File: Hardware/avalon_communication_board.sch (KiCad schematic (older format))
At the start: 22 parts, among them IC1 ENC28J60-I/SO, J1 RJ45_LEDS, P1 B2P-VH, Q1 FMMT597, Q2 BC817, Q3 BC817, Q4 FMMT597, Q5 BC817

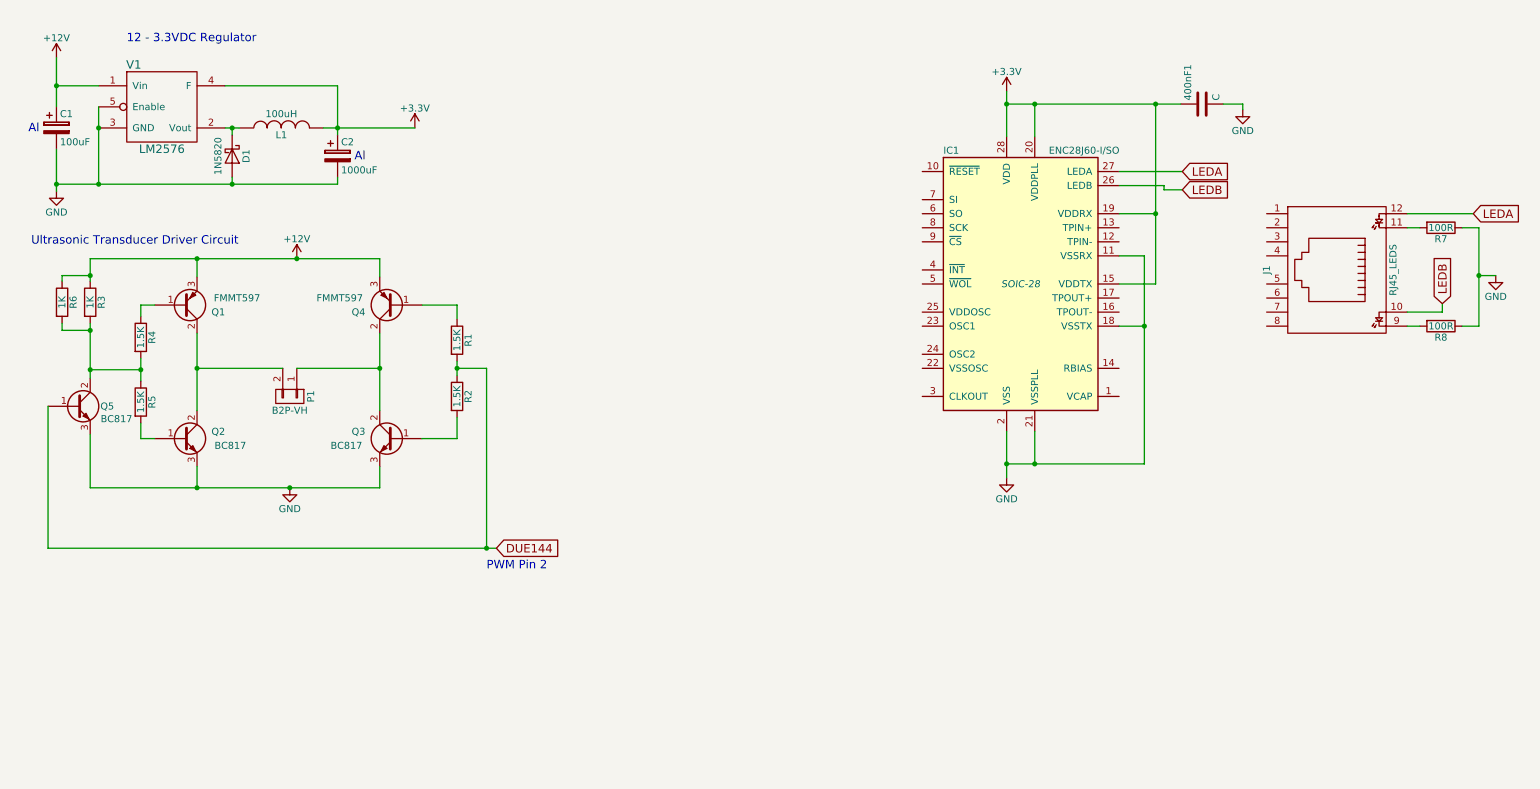
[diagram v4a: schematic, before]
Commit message: -Continued work on Ethernet Controller
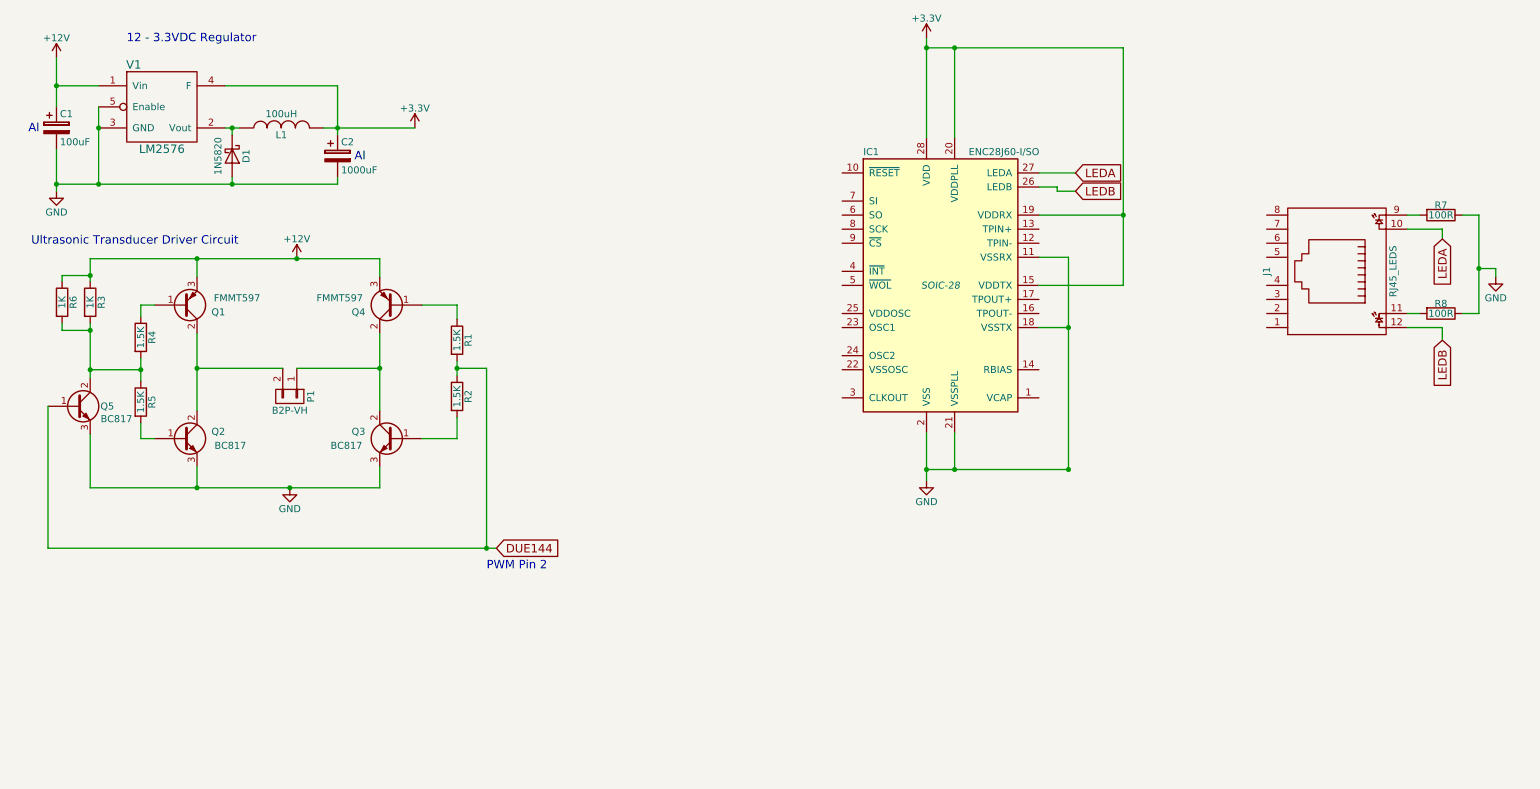
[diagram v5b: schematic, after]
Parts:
- removed 400nF1: C, symbol C
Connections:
- net LEDA: now also J1.10; no longer J1.12
- net LEDB: now also J1.12; no longer J1.10
- net at J1.11: now also R8.2; no longer R7.2
- net at J1.9: now also R7.2; no longer R8.2
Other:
- moved on the sheet: IC1, R7, R8
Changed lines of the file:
@@
 $EndComp
 Wire Wire Line
-	1040 2440 1040 2280
+	1040 2280 1040 2440
 Wire Wire Line
 	1040 2280 3100 2280
@@
 L ENC28J60-I/SO IC1
 U 1 1 5A903E11
-P 7660 2460
-F 0 "IC1" H 7110 3410 50  0000 L CNN
-F 1 "ENC28J60-I/SO" H 7860 3410 50  0000 L CNN
-F 2 "SOIC-28" H 7660 2460 50  0000 C CIN
-F 3 "" H 7660 2460 50  0000 C CNN
-	1    7660 2460
+P 7090 2470
+F 0 "IC1" H 6540 3420 50  0000 L CNN
+F 1 "ENC28J60-I/SO" H 7290 3420 50  0000 L CNN
+F 2 "SOIC-28" H 7090 2470 50  0000 C CIN
+F 3 "" H 7090 2470 50  0000 C CNN
+	1    7090 2470
 	1    0    0    -1
 $EndComp
@@
 L RJ45_LEDS J1
 U 1 1 5A9063FA
-P 9910 2360
-F 0 "J1" H 9910 1860 50  0000 C CNN
-F 1 "RJ45_LEDS" H 9910 2760 50  0000 C CNN
-F 2 "" H 9910 2310 50  0000 C CNN
-F 3 "" H 9910 2310 50  0000 C CNN
-	1    9910 2360
-	0    1    1    0
+P 9910 2370
+F 0 "J1" H 9910 1870 50  0000 C CNN
+F 1 "RJ45_LEDS" H 9910 2770 50  0000 C CNN
+F 2 "" H 9910 2320 50  0000 C CNN
+F 3 "" H 9910 2320 50  0000 C CNN
+	1    9910 2370
+	0    1    -1   0
 $EndComp
 $Comp
@@
 L +3.3V #PWR6
 U 1 1 5A908CDC
-P 7560 1090
-F 0 "#PWR6" H 7560 940 50  0001 C CNN
-F 1 "+3.3V" H 7560 1230 50  0000 C CNN
-F 2 "" H 7560 1090 50  0000 C CNN
-F 3 "" H 7560 1090 50  0000 C CNN
-	1    7560 1090
-	1    0    0    -1
-$EndComp
-Wire Wire Line
-	7560 1090 7560 1410
-Wire Wire Line
-	7760 1410 7760 1180
-Connection ~ 7560 1180
-Wire Wire Line
-	8360 1960 8620 1960
-Wire Wire Line
-	8620 1180 8620 2460
-Connection ~ 7760 1180
-Wire Wire Line
-	8620 2460 8360 2460
-Connection ~ 8620 1960
+P 6990 710
+F 0 "#PWR6" H 6990 560 50  0001 C CNN
+F 1 "+3.3V" H 6990 850 50  0000 C CNN
+F 2 "" H 6990 710 50  0000 C CNN
+F 3 "" H 6990 710 50  0000 C CNN
+	1    6990 710
+	1    0    0    -1
+$EndComp
 $Comp
 L GND #PWR7
 U 1 1 5A90B1AB
-P 7560 3840
-F 0 "#PWR7" H 7560 3590 50  0001 C CNN
-F 1 "GND" H 7560 3690 50  0000 C CNN
-F 2 "" H 7560 3840 50  0000 C CNN
-F 3 "" H 7560 3840 50  0000 C CNN
-	1    7560 3840
-	1    0    0    -1
-$EndComp
-Wire Wire Line
-	7560 3510 7560 3840
-Wire Wire Line
-	7760 3510 7760 3740
-Wire Wire Line
-	8540 3740 7560 3740
-Connection ~ 7560 3740
-Wire Wire Line
-	8540 2260 8540 3740
-Wire Wire Line
-	8540 2760 8360 2760
-Connection ~ 7760 3740
-Wire Wire Line
-	8540 2260 8360 2260
-Connection ~ 8540 2760
-Wire Wire Line
-	7560 1180 8800 1180
-$Comp
-L C 400nF1
-U 1 1 5A90F1A9
-P 8950 1180
-F 0 "400nF1" H 8975 1280 50  0000 L CNN
-F 1 "C" H 8975 1080 50  0000 L CNN
-F 2 "" H 8988 1030 50  0000 C CNN
-F 3 "" H 8950 1180 50  0000 C CNN
-	1    8950 1180
-	0    -1   -1   0
-$EndComp
-Connection ~ 8620 1180
-$Comp
-L GND #PWR8
-U 1 1 5A90F671
-P 9240 1220
-F 0 "#PWR8" H 9240 970 50  0001 C CNN
-F 1 "GND" H 9240 1070 50  0000 C CNN
-F 2 "" H 9240 1220 50  0000 C CNN
-F 3 "" H 9240 1220 50  0000 C CNN
-	1    9240 1220
-	1    0    0    -1
-$EndComp
-Wire Wire Line
-	9100 1180 9240 1180
-Wire Wire Line
-	9240 1180 9240 1220
-Text GLabel 8810 1660 2    60   Input ~ 0
+P 6990 3860
+F 0 "#PWR7" H 6990 3610 50  0001 C CNN
+F 1 "GND" H 6990 3710 50  0000 C CNN
+F 2 "" H 6990 3860 50  0000 C CNN
+F 3 "" H 6990 3860 50  0000 C CNN
+	1    6990 3860
+	1    0    0    -1
+$EndComp
+Text GLabel 8050 1670 2    60   Input ~ 0
 LEDA
-Wire Wire Line
-	8360 1660 8810 1660
-Text GLabel 8810 1790 2    60   Input ~ 0
+Text GLabel 8050 1800 2    60   Input ~ 0
 LEDB
-Wire Wire Line
-	8360 1760 8680 1760
-Wire Wire Line
-	8680 1760 8680 1790
-Wire Wire Line
-	8680 1790 8810 1790
 $Comp
 L R R7
 U 1 1 5A911D20
-P 10650 2060
-F 0 "R7" V 10730 2060 50  0000 C CNN
-F 1 "100R" V 10650 2060 50  0000 C CNN
-F 2 "" V 10580 2060 50  0000 C CNN
-F 3 "" H 10650 2060 50  0000 C CNN
-	1    10650 2060
+P 10650 1970
+F 0 "R7" V 10580 1970 50  0000 C CNN
+F 1 "100R" V 10650 1970 50  0000 C CNN
+F 2 "" V 10580 1970 50  0000 C CNN
+F 3 "" H 10650 1970 50  0000 C CNN
+	1    10650 1970
 	0    1    1    0
 $EndComp
@@
 L R R8
 U 1 1 5A91211B
-P 10650 2760
-F 0 "R8" V 10730 2760 50  0000 C CNN
-F 1 "100R" V 10650 2760 50  0000 C CNN
-F 2 "" V 10580 2760 50  0000 C CNN
-F 3 "" H 10650 2760 50  0000 C CNN
-	1    10650 2760
+P 10650 2670
+F 0 "R8" V 10580 2670 50  0000 C CNN
+F 1 "100R" V 10650 2670 50  0000 C CNN
+F 2 "" V 10580 2670 50  0000 C CNN
+F 3 "" H 10650 2670 50  0000 C CNN
+	1    10650 2670
 	0    1    1    0
 $EndComp
-Wire Wire Line
-	10410 2060 10500 2060
-Text GLabel 10880 1960 2    60   Input ~ 0
+Text GLabel 10660 2140 3    60   Input ~ 0
 LEDA
-Wire Wire Line
-	10410 1960 10880 1960
 $Comp
 L GND #PWR9
 U 1 1 5A913778
-P 11040 2400
-F 0 "#PWR9" H 11040 2150 50  0001 C CNN
-F 1 "GND" H 11040 2250 50  0000 C CNN
-F 2 "" H 11040 2400 50  0000 C CNN
-F 3 "" H 11040 2400 50  0000 C CNN
-	1    11040 2400
-	1    0    0    -1
-$EndComp
-Wire Wire Line
-	10800 2060 10920 2060
-Wire Wire Line
-	10920 2060 10920 2760
-Wire Wire Line
-	10920 2400 11040 2400
-Connection ~ 10920 2400
-Wire Wire Line
-	10920 2760 10800 2760
-Wire Wire Line
-	10500 2760 10410 2760
-Text GLabel 10660 2600 1    60   Input ~ 0
+P 11040 2410
+F 0 "#PWR9" H 11040 2160 50  0001 C CNN
+F 1 "GND" H 11040 2260 50  0000 C CNN
+F 2 "" H 11040 2410 50  0000 C CNN
+F 3 "" H 11040 2410 50  0000 C CNN
+	1    11040 2410
+	1    0    0    -1
+$EndComp
+Text GLabel 10660 2860 3    60   Input ~ 0
 LEDB
 Wire Wire Line
-	10410 2660 10660 2660
-Wire Wire Line
-	10660 2660 10660 2600
+	10410 2770 10660 2770
+Wire Wire Line
+	10660 2770 10660 2860
+Wire Wire Line
+	10920 2670 10800 2670
+Wire Wire Line
+	10800 1970 10920 1970
+Wire Wire Line
+	10920 1970 10920 2670
+Wire Wire Line
+	11040 2410 11040 2350
+Wire Wire Line
+	11040 2350 10920 2350
+Connection ~ 10920 2350
+Wire Wire Line
+	10410 2670 10500 2670
+Wire Wire Line
+	10410 1970 10500 1970
+Wire Wire Line
+	10410 2070 10660 2070
+Wire Wire Line
+	10660 2070 10660 2140
+Wire Wire Line
+	6990 780  8390 780
+Wire Wire Line
+	7790 1670 8050 1670
+Wire Wire Line
+	7790 1770 7920 1770
+Wire Wire Line
+	7920 1770 7920 1800
+Wire Wire Line
+	7920 1800 8050 1800
+Wire Wire Line
+	7790 1970 8390 1970
+Wire Wire Line
+	8390 780  8390 2470
+Wire Wire Line
+	6990 710  6990 1420
+Connection ~ 6990 780
+Wire Wire Line
+	7190 1420 7190 780
+Connection ~ 7190 780
+Wire Wire Line
+	8390 2470 7790 2470
+Connection ~ 8390 1970
+Wire Wire Line
+	6990 3520 6990 3860
+Wire Wire Line
+	7190 3520 7190 3780
+Wire Wire Line
+	8000 3780 6990 3780
+Connection ~ 6990 3780
+Wire Wire Line
+	7790 2270 8000 2270
+Wire Wire Line
+	8000 2270 8000 3780
+Wire Wire Line
+	8000 2770 7790 2770
+Connection ~ 8000 2770
+Connection ~ 7190 3780
+Connection ~ 8000 3780
 $EndSCHEMATC

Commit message: -Continued work on the ethernet controller
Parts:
- added U?: B78476A8247A003, symbol B78476A8247A003
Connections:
- net at IC1.12 (TPIN-): now also U?.3 (TD-)
- net at IC1.13 (TPIN+): now also U?.1 (TD+)
- net at IC1.16 (TPOUT-): now also U?.8 (RD-)
- net at IC1.17 (TPOUT+): now also U?.6 (RD+)
- net CAM2B: now reaches J1.4
- net at J1.5: now also U?.9 (RX-)
- net at J1.6: now also U?.11 (RX+)
- net at J1.7: now also U?.14 (TX-)
- net at J1.8: now also U?.16 (TX+)
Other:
- moved on the sheet: IC1
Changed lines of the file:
@@
 L ENC28J60-I/SO IC1
 U 1 1 5A903E11
-P 7090 2470
-F 0 "IC1" H 6540 3420 50  0000 L CNN
-F 1 "ENC28J60-I/SO" H 7290 3420 50  0000 L CNN
-F 2 "SOIC-28" H 7090 2470 50  0000 C CIN
-F 3 "" H 7090 2470 50  0000 C CNN
-	1    7090 2470
+P 6280 2470
+F 0 "IC1" H 5730 3420 50  0000 L CNN
+F 1 "ENC28J60-I/SO" H 6480 3420 50  0000 L CNN
+F 2 "SOIC-28" H 6280 2470 50  0000 C CIN
+F 3 "" H 6280 2470 50  0000 C CNN
+	1    6280 2470
 	1    0    0    -1
 $EndComp
@@
 L +3.3V #PWR6
 U 1 1 5A908CDC
-P 6990 710
-F 0 "#PWR6" H 6990 560 50  0001 C CNN
-F 1 "+3.3V" H 6990 850 50  0000 C CNN
-F 2 "" H 6990 710 50  0000 C CNN
-F 3 "" H 6990 710 50  0000 C CNN
-	1    6990 710
+P 6180 710
+F 0 "#PWR6" H 6180 560 50  0001 C CNN
+F 1 "+3.3V" H 6180 850 50  0000 C CNN
+F 2 "" H 6180 710 50  0000 C CNN
+F 3 "" H 6180 710 50  0000 C CNN
+	1    6180 710
 	1    0    0    -1
 $EndComp
@@
 L GND #PWR7
 U 1 1 5A90B1AB
-P 6990 3860
-F 0 "#PWR7" H 6990 3610 50  0001 C CNN
-F 1 "GND" H 6990 3710 50  0000 C CNN
-F 2 "" H 6990 3860 50  0000 C CNN
-F 3 "" H 6990 3860 50  0000 C CNN
-	1    6990 3860
-	1    0    0    -1
-$EndComp
-Text GLabel 8050 1670 2    60   Input ~ 0
+P 6180 3860
+F 0 "#PWR7" H 6180 3610 50  0001 C CNN
+F 1 "GND" H 6180 3710 50  0000 C CNN
+F 2 "" H 6180 3860 50  0000 C CNN
+F 3 "" H 6180 3860 50  0000 C CNN
+	1    6180 3860
+	1    0    0    -1
+$EndComp
+Text GLabel 7240 1670 2    60   Input ~ 0
 LEDA
-Text GLabel 8050 1800 2    60   Input ~ 0
+Text GLabel 7240 1800 2    60   Input ~ 0
 LEDB
 $Comp
@@
 	10660 2070 10660 2140
 Wire Wire Line
-	6990 780  8390 780
-Wire Wire Line
-	7790 1670 8050 1670
-Wire Wire Line
-	7790 1770 7920 1770
-Wire Wire Line
-	7920 1770 7920 1800
-Wire Wire Line
-	7920 1800 8050 1800
-Wire Wire Line
-	7790 1970 8390 1970
-Wire Wire Line
-	8390 780  8390 2470
-Wire Wire Line
-	6990 710  6990 1420
-Connection ~ 6990 780
-Wire Wire Line
-	7190 1420 7190 780
-Connection ~ 7190 780
-Wire Wire Line
-	8390 2470 7790 2470
-Connection ~ 8390 1970
-Wire Wire Line
-	6990 3520 6990 3860
-Wire Wire Line
-	7190 3520 7190 3780
-Wire Wire Line
-	8000 3780 6990 3780
-Connection ~ 6990 3780
-Wire Wire Line
-	7790 2270 8000 2270
-Wire Wire Line
-	8000 2270 8000 3780
-Wire Wire Line
-	8000 2770 7790 2770
-Connection ~ 8000 2770
+	6180 780  7580 780
+Wire Wire Line
+	6980 1670 7240 1670
+Wire Wire Line
+	6980 1770 7110 1770
+Wire Wire Line
+	7110 1770 7110 1800
+Wire Wire Line
+	7110 1800 7240 1800
+Wire Wire Line
+	6980 1970 7580 1970
+Wire Wire Line
+	7580 780  7580 2470
+Wire Wire Line
+	6180 710  6180 1420
+Connection ~ 6180 780
+Wire Wire Line
+	6380 1420 6380 780
+Connection ~ 6380 780
+Wire Wire Line
+	7580 2470 6980 2470
+Connection ~ 7580 1970
+Wire Wire Line
+	6180 3520 6180 3860
+Wire Wire Line
+	6380 3520 6380 3780
+Wire Wire Line
+	7190 3780 6180 3780
+Connection ~ 6180 3780
+Wire Wire Line
+	6980 2270 7190 2270
+Wire Wire Line
+	7190 2270 7190 3780
+Wire Wire Line
+	7190 2770 6980 2770
+Connection ~ 7190 2770
+Connection ~ 6380 3780
 Connection ~ 7190 3780
-Connection ~ 8000 3780
+$Comp
+L B78476A8247A003 U?
+U 1 1 5A907D1C
+P 8290 2290
+F 0 "U?" H 7990 2590 60  0000 C CNN
+F 1 "B78476A8247A003" H 8290 1790 60  0000 C CNN
+F 2 "" H 8290 2290 60  0001 C CNN
+F 3 "" H 8290 2290 60  0001 C CNN
+	1    8290 2290
+	1    0    0    -1
+$EndComp
+Wire Wire Line
+	8840 1970 9410 1970
+Wire Wire Line
+	8925 2070 9410 2070
+Wire Wire Line
+	8925 2070 8925 2340
+Wire Wire Line
+	8840 2440 9015 2440
+Wire Wire Line
+	8955 2270 9410 2270
+Wire Wire Line
+	8925 2340 8840 2340
+Wire Wire Line
+	6980 2070 7345 2070
+Wire Wire Line
+	7345 2070 7345 2140
+Wire Wire Line
+	7345 2140 7740 2140
+Wire Wire Line
+	7345 2340 7740 2340
+Wire Wire Line
+	7345 2340 7345 2170
+Wire Wire Line
+	7345 2170 6980 2170
+Wire Wire Line
+	6980 2570 7410 2570
+Wire Wire Line
+	7410 2570 7410 2440
+Wire Wire Line
+	7410 2440 7740 2440
+Wire Wire Line
+	6980 2670 7410 2670
+Wire Wire Line
+	7410 2670 7410 2640
+Wire Wire Line
+	7410 2640 7740 2640
+Text GLabel 9265 3040 3    60   Input ~ 0
+CAM1A
+Text GLabel 9390 3040 3    60   Input ~ 0
+CAM1B
+Text GLabel 9140 3040 3    60   Input ~ 0
+CAM2A
+Text GLabel 9015 3040 3    60   Input ~ 0
+CAM2B
+Wire Wire Line
+	8955 2640 8840 2640
+Wire Wire Line
+	8955 2270 8955 2640
+Wire Wire Line
+	9015 2470 9015 3040
+Wire Wire Line
+	9015 2440 9015 2170
+Wire Wire Line
+	9015 2170 9410 2170
+Wire Wire Line
+	9015 2470 9410 2470
+Wire Wire Line
+	8840 1970 8840 2140
 $EndSCHEMATC
